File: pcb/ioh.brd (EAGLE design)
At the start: 100 x 80 mm, 11 parts, among them Q1 MOSFET-NCHANNEL2N7000

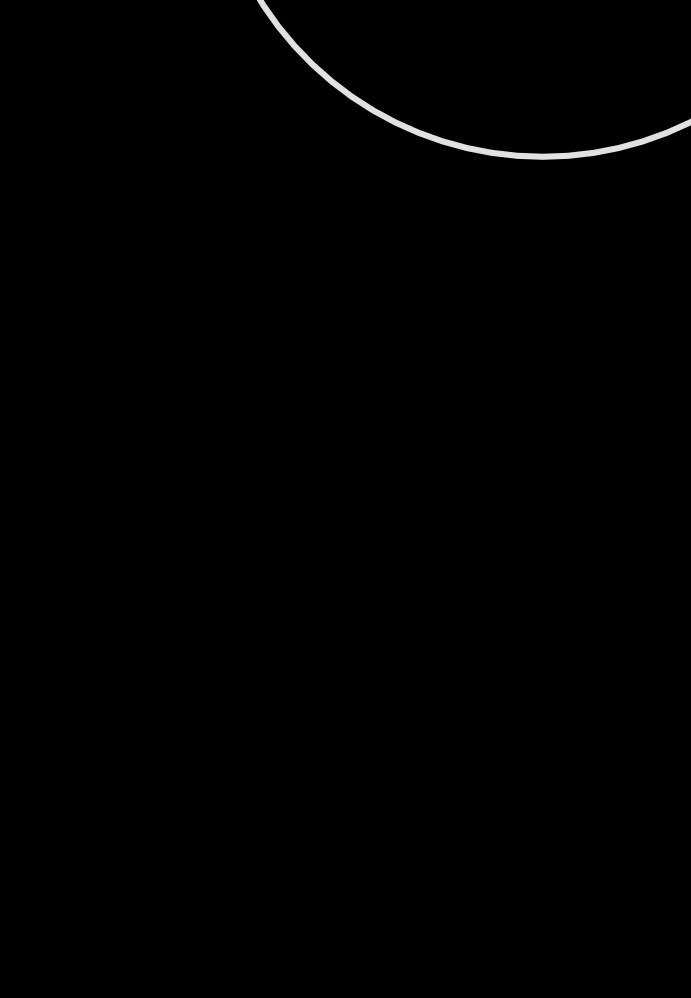
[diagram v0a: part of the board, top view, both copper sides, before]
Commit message: add front/back tx
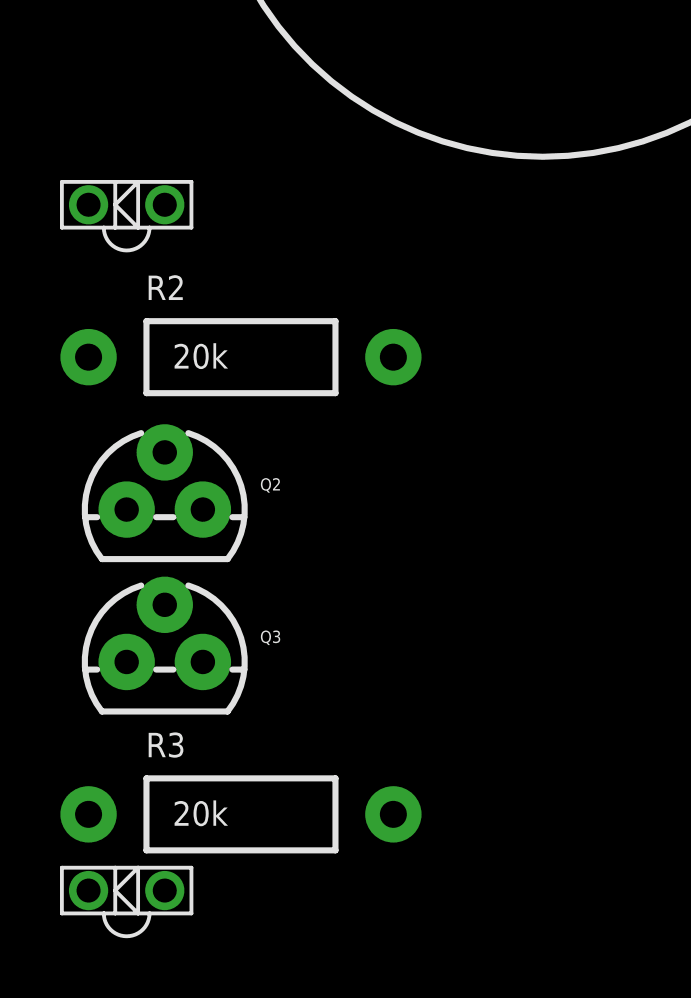
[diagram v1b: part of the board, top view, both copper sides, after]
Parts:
- added D1, D2: (no value), SparkFun-LED:LTE-302
- added Q2, Q3: MOSFET-NCHANNEL2N7000, SparkFun-DiscreteSemi:TO-92
- added R2, R3: 20k, SparkFun-Resistors:AXIAL-0.4
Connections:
- new net N$11: D1.C, Q2.3
- new net N$24: D2.A, R3.P$1
- new net N$25: D2.C, Q3.3
- new net N$4: D1.A, R2.P$1
- new net TXBACK: Q3.2
- new net TXFRONT: Q2.2
- net GND: now also Q2.1, Q3.1
- net VCC: now also R2.P$2, R3.P$2
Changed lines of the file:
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@@
 <element name="Q1" library="SparkFun-DiscreteSemi" package="TO-92" value="MOSFET-NCHANNEL2N7000" x="-52.07" y="71.12"/>
 <element name="R1" library="SparkFun-Resistors" package="AXIAL-0.4" value="20k" x="-62.23" y="69.85"/>
+<element name="D1" library="SparkFun-LED" package="LTE-302" value="" x="-66.04" y="-1.27"/>
+<element name="R2" library="SparkFun-Resistors" package="AXIAL-0.4" value="20k" x="-62.23" y="-6.35"/>
+<element name="Q2" library="SparkFun-DiscreteSemi" package="TO-92" value="MOSFET-NCHANNEL2N7000" x="-64.77" y="-11.43"/>
+<element name="D2" library="SparkFun-LED" package="LTE-302" value="" x="-66.04" y="-24.13"/>
+<element name="R3" library="SparkFun-Resistors" package="AXIAL-0.4" value="20k" x="-62.23" y="-21.59"/>
+<element name="Q3" library="SparkFun-DiscreteSemi" package="TO-92" value="MOSFET-NCHANNEL2N7000" x="-64.77" y="-16.51"/>
 </elements>
 <signals>
@@
 <contactref element="LED3" pad="VSS"/>
 <contactref element="Q1" pad="1"/>
+<contactref element="Q2" pad="1"/>
+<contactref element="Q3" pad="1"/>
+<wire x1="-66.04" y1="-11.43" x2="-66.04" y2="-16.51" width="0" layer="19" extent="1-1"/>
+<wire x1="-60.22" y1="11.43" x2="-66.04" y2="-11.43" width="0" layer="19" extent="1-1"/>
 <wire x1="-36.4" y1="9.62" x2="-60.22" y2="11.43" width="0" layer="19" extent="1-1"/>
 <wire x1="-60.42" y1="38.94" x2="-60.22" y2="11.43" width="0" layer="19" extent="1-1"/>
@@
 <contactref element="LED2" pad="VDD"/>
 <contactref element="R1" pad="P$2"/>
-<wire x1="-21.05" y1="63.5" x2="-17.05" y2="65.2" width="0" layer="19" extent="1-1"/>
-<wire x1="-25.94" y1="65.2" x2="-21.05" y2="63.5" width="0" layer="19" extent="1-1"/>
-<wire x1="-29.94" y1="63.5" x2="-25.94" y2="65.2" width="0" layer="19" extent="1-1"/>
+<contactref element="R2" pad="P$2"/>
+<contactref element="R3" pad="P$2"/>
+<wire x1="-57.15" y1="-6.35" x2="-57.15" y2="-21.59" width="0" layer="19" extent="1-1"/>
+<wire x1="-60.42" y1="40.64" x2="-57.15" y2="-6.35" width="0" layer="19" extent="1-1"/>
+<wire x1="-56.42" y1="42.34" x2="-60.42" y2="40.64" width="0" layer="19" extent="1-1"/>
+<wire x1="-51.53" y1="40.64" x2="-56.42" y2="42.34" width="0" layer="19" extent="1-1"/>
+<wire x1="-47.53" y1="42.34" x2="-51.53" y2="40.64" width="0" layer="19" extent="1-1"/>
+<wire x1="-29.94" y1="63.5" x2="-47.53" y2="42.34" width="0" layer="19" extent="1-1"/>
+<wire x1="-25.94" y1="65.2" x2="-29.94" y2="63.5" width="0" layer="19" extent="1-1"/>
+<wire x1="-21.05" y1="63.5" x2="-25.94" y2="65.2" width="0" layer="19" extent="1-1"/>
+<wire x1="-17.05" y1="65.2" x2="-21.05" y2="63.5" width="0" layer="19" extent="1-1"/>
 <wire x1="-14.82" y1="46.99" x2="-21.05" y2="63.5" width="0" layer="19" extent="1-1"/>
-<wire x1="-47.53" y1="42.34" x2="-29.94" y2="63.5" width="0" layer="19" extent="1-1"/>
-<wire x1="-51.53" y1="40.64" x2="-47.53" y2="42.34" width="0" layer="19" extent="1-1"/>
-<wire x1="-56.42" y1="42.34" x2="-51.53" y2="40.64" width="0" layer="19" extent="1-1"/>
-<wire x1="-60.42" y1="40.64" x2="-56.42" y2="42.34" width="0" layer="19" extent="1-1"/>
 <wire x1="-57.15" y1="69.85" x2="-56.42" y2="42.34" width="0" layer="19" extent="1-1"/>
 </signal>
@@
 <wire x1="-47.53" y1="40.64" x2="-50.8" y2="71.12" width="0" layer="19" extent="1-1"/>
 </signal>
+<signal name="N$4">
+<contactref element="R2" pad="P$1"/>
+<contactref element="D1" pad="A"/>
+<wire x1="-64.77" y1="-1.27" x2="-67.31" y2="-6.35" width="0" layer="19" extent="1-1"/>
+</signal>
+<signal name="N$11">
+<contactref element="D1" pad="C"/>
+<contactref element="Q2" pad="3"/>
+<wire x1="-67.31" y1="-1.27" x2="-63.5" y2="-11.43" width="0" layer="19" extent="1-1"/>
+</signal>
+<signal name="TXBACK">
+<contactref element="Q3" pad="2"/>
+</signal>
+<signal name="N$24">
+<contactref element="R3" pad="P$1"/>
+<contactref element="D2" pad="A"/>
+<wire x1="-64.77" y1="-24.13" x2="-67.31" y2="-21.59" width="0" layer="19" extent="1-1"/>
+</signal>
+<signal name="N$25">
+<contactref element="D2" pad="C"/>
+<contactref element="Q3" pad="3"/>
+<wire x1="-63.5" y1="-16.51" x2="-67.31" y2="-24.13" width="0" layer="19" extent="1-1"/>
+</signal>
+<signal name="TXFRONT">
+<contactref element="Q2" pad="2"/>
+</signal>
 </signals>

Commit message: tsop library addition; placement
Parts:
- added RXBACK, RXFRONT: TSOP2438, ioh-1:TSOP2438
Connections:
- new net RXBACK: RXBACK.OUT
- new net RXFRONT: RXFRONT.OUT
- net GND: now also RXBACK.GND, RXFRONT.GND
- net VCCIO: now also RXBACK.VS, RXFRONT.VS
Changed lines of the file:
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@@
 <element name="R3" library="SparkFun-Resistors" package="AXIAL-0.4" value="20k" x="-62.23" y="-21.59"/>
 <element name="Q3" library="SparkFun-DiscreteSemi" package="TO-92" value="MOSFET-NCHANNEL2N7000" x="-64.77" y="-16.51"/>
+<element name="RXFRONT" library="ioh-1" package="TSOP2438" value="TSOP2438" x="-63.5" y="-27.94"/>
+<element name="RXBACK" library="ioh-1" package="TSOP2438" value="TSOP2438" x="-63.5" y="-33.02"/>
 </elements>
 <signals>
@@
 <contactref element="Q2" pad="1"/>
 <contactref element="Q3" pad="1"/>
+<contactref element="RXFRONT" pad="GND"/>
+<contactref element="RXFRONT" pad="GND"/>
+<contactref element="RXBACK" pad="GND"/>
+<contactref element="RXBACK" pad="GND"/>
+<wire x1="-63.5" y1="-27.94" x2="-63.5" y2="-33.02" width="0" layer="19" extent="1-1"/>
+<wire x1="-66.04" y1="-16.51" x2="-63.5" y2="-27.94" width="0" layer="19" extent="1-1"/>
 <wire x1="-66.04" y1="-11.43" x2="-66.04" y2="-16.51" width="0" layer="19" extent="1-1"/>
 <wire x1="-60.22" y1="11.43" x2="-66.04" y2="-11.43" width="0" layer="19" extent="1-1"/>
@@
 <contactref element="JP1" pad="1"/>
 <contactref element="U$1" pad="1"/>
+<contactref element="RXFRONT" pad="VS"/>
+<contactref element="RXBACK" pad="VS"/>
+<wire x1="-60.96" y1="-27.94" x2="-60.96" y2="-33.02" width="0" layer="19" extent="1-1"/>
+<wire x1="-40.22" y1="11.43" x2="-60.96" y2="-27.94" width="0" layer="19" extent="1-1"/>
 <wire x1="-36.4" y1="27.62" x2="-40.22" y2="11.43" width="0" layer="19" extent="1-1"/>
 <wire x1="-34.82" y1="46.99" x2="-36.4" y2="27.62" width="0" layer="19" extent="1-1"/>
@@
 <contactref element="Q2" pad="2"/>
 </signal>
+<signal name="RXFRONT">
+<contactref element="RXFRONT" pad="OUT"/>
+</signal>
+<signal name="RXBACK">
+<contactref element="RXBACK" pad="OUT"/>
+</signal>
 </signals>

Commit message: vibe placement; update todo; caps
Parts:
- added C1: 10uF, SparkFun-Capacitors:CPOL-RADIAL-10UF-25V-KIT
- added JP3: M02PTH, SparkFun-Connectors:1X02
- added Q4: MOSFET-NCHANNEL2N7000, SparkFun-DiscreteSemi:TO-92
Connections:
- new net N$13: JP3.2, Q4.3
- new net VIBE: Q4.2
- net GND: now also C1.2, Q4.1
- net VCC: now also JP3.1
- net VCCIO: now also C1.1
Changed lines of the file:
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@@
 <element name="RXFRONT" library="ioh-1" package="TSOP2438" value="TSOP2438" x="-63.5" y="-27.94"/>
 <element name="RXBACK" library="ioh-1" package="TSOP2438" value="TSOP2438" x="-63.5" y="-33.02"/>
+<element name="C1" library="SparkFun-Capacitors" package="CPOL-RADIAL-10UF-25V-KIT" value="10uF" x="-72.39" y="-30.48">
+<attribute name="PROD_ID" value="CAP-08440" x="-72.39" y="-30.48" size="1.778" layer="27" display="off"/>
+</element>
+<element name="JP3" library="SparkFun-Connectors" package="1X02" value="M02PTH" x="-72.39" y="-39.37"/>
+<element name="Q4" library="SparkFun-DiscreteSemi" package="TO-92" value="MOSFET-NCHANNEL2N7000" x="-71.12" y="-46.99"/>
 </elements>
 <signals>
@@
 <contactref element="RXBACK" pad="GND"/>
 <contactref element="RXBACK" pad="GND"/>
+<contactref element="C1" pad="2"/>
+<contactref element="Q4" pad="1"/>
+<wire x1="-73.66" y1="-30.48" x2="-72.39" y2="-46.99" width="0" layer="19" extent="1-1"/>
+<wire x1="-63.5" y1="-33.02" x2="-73.66" y2="-30.48" width="0" layer="19" extent="1-1"/>
 <wire x1="-63.5" y1="-27.94" x2="-63.5" y2="-33.02" width="0" layer="19" extent="1-1"/>
 <wire x1="-66.04" y1="-16.51" x2="-63.5" y2="-27.94" width="0" layer="19" extent="1-1"/>
@@
 <contactref element="RXFRONT" pad="VS"/>
 <contactref element="RXBACK" pad="VS"/>
+<contactref element="C1" pad="1"/>
+<wire x1="-60.96" y1="-33.02" x2="-71.12" y2="-30.48" width="0" layer="19" extent="1-1"/>
 <wire x1="-60.96" y1="-27.94" x2="-60.96" y2="-33.02" width="0" layer="19" extent="1-1"/>
 <wire x1="-40.22" y1="11.43" x2="-60.96" y2="-27.94" width="0" layer="19" extent="1-1"/>
@@
 <contactref element="R2" pad="P$2"/>
 <contactref element="R3" pad="P$2"/>
+<contactref element="JP3" pad="1"/>
+<wire x1="-57.15" y1="-21.59" x2="-72.39" y2="-39.37" width="0" layer="19" extent="1-1"/>
 <wire x1="-57.15" y1="-6.35" x2="-57.15" y2="-21.59" width="0" layer="19" extent="1-1"/>
 <wire x1="-60.42" y1="40.64" x2="-57.15" y2="-6.35" width="0" layer="19" extent="1-1"/>
@@
 <contactref element="RXBACK" pad="OUT"/>
 </signal>
+<signal name="N$13">
+<contactref element="Q4" pad="3"/>
+<contactref element="JP3" pad="2"/>
+<wire x1="-69.85" y1="-39.37" x2="-69.85" y2="-46.99" width="0" layer="19" extent="1-1"/>
+</signal>
+<signal name="VIBE">
+<contactref element="Q4" pad="2"/>
+</signal>
 </signals>

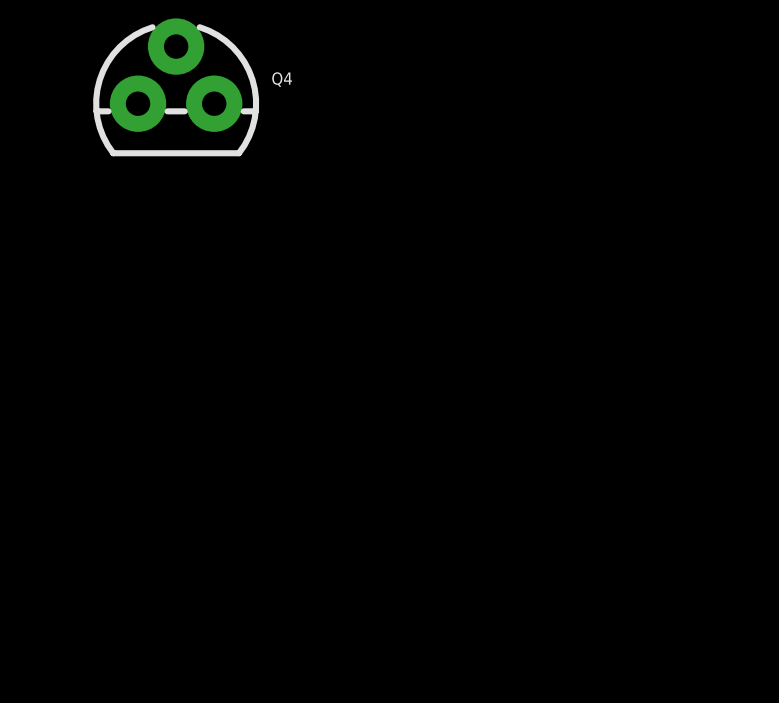
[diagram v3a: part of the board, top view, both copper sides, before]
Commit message: add switch
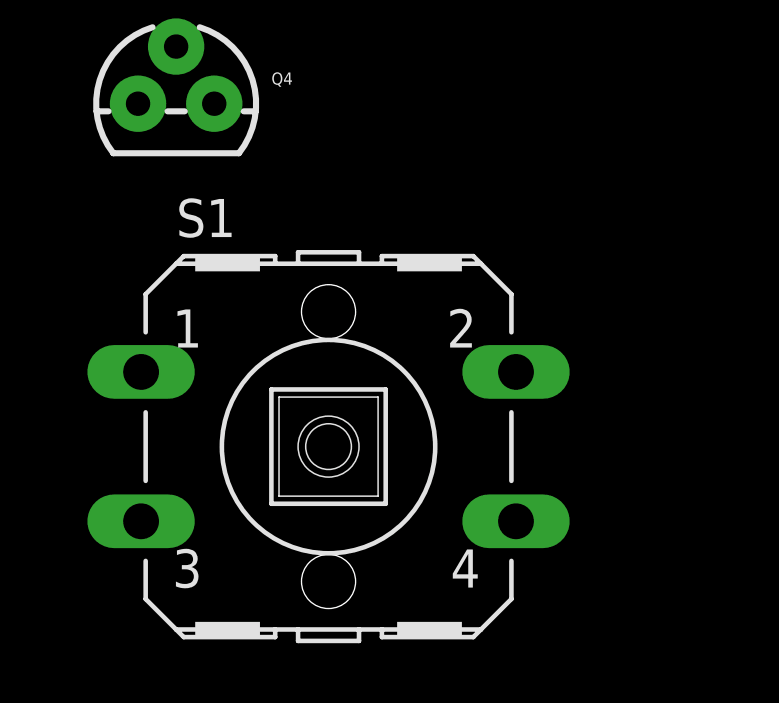
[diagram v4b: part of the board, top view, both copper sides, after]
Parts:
- added S1: (no value), adafruit:B3F-40XX
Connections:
- new net BOOP: S1.1, S1.2
- net GND: now also S1.3, S1.4
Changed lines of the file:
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@@
 <element name="JP3" library="SparkFun-Connectors" package="1X02" value="M02PTH" x="-72.39" y="-39.37"/>
 <element name="Q4" library="SparkFun-DiscreteSemi" package="TO-92" value="MOSFET-NCHANNEL2N7000" x="-71.12" y="-46.99"/>
+<element name="S1" library="adafruit" package="B3F-40XX" value="" x="-66.04" y="-58.42">
+<attribute name="OC_NEWARK" value="36K3105" x="-66.04" y="-58.42" size="1.778" layer="27" display="off"/>
+<attribute name="MPN" value="B3F-4000" x="-66.04" y="-58.42" size="1.778" layer="27" display="off"/>
+<attribute name="MF" value="OMRON COMPONENTS USA" x="-66.04" y="-58.42" size="1.778" layer="27" display="off"/>
+<attribute name="OC_FARNELL" value="176434" x="-66.04" y="-58.42" size="1.778" layer="27" display="off"/>
+</element>
 </elements>
 <signals>
@@
 <contactref element="C1" pad="2"/>
 <contactref element="Q4" pad="1"/>
+<contactref element="S1" pad="3"/>
+<contactref element="S1" pad="4"/>
+<wire x1="-59.7916" y1="-60.9092" x2="-72.2884" y2="-60.9092" width="0" layer="19" extent="1-1"/>
+<wire x1="-72.39" y1="-46.99" x2="-72.2884" y2="-60.9092" width="0" layer="19" extent="1-1"/>
 <wire x1="-73.66" y1="-30.48" x2="-72.39" y2="-46.99" width="0" layer="19" extent="1-1"/>
 <wire x1="-63.5" y1="-33.02" x2="-73.66" y2="-30.48" width="0" layer="19" extent="1-1"/>
@@
 <contactref element="Q4" pad="2"/>
 </signal>
+<signal name="BOOP">
+<contactref element="S1" pad="1"/>
+<contactref element="S1" pad="2"/>
+<wire x1="-59.7916" y1="-55.9308" x2="-72.2884" y2="-55.9308" width="0" layer="19" extent="1-1"/>
+</signal>
 </signals>

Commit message: actually connect things
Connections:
- removed net N$15: JP2.2, U$1.12
- removed net N$17: JP2.4, U$1.14
- removed net N$20: JP2.7, U$1.17
- removed net N$21: JP2.8, U$1.18
- removed net N$6: JP1.3, U$1.3
- net RXBACK: now also JP2.4, U$1.14
- net RXFRONT: now also JP1.3, U$1.3
- net TXBACK: now also JP2.7, U$1.17
- net TXFRONT: now also JP2.8, U$1.18
- net VIBE: now also JP2.2, U$1.12
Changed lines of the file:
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@@
 <wire x1="-53.34" y1="62.23" x2="-36.4" y2="25.62" width="0" layer="19" extent="1-1"/>
-</signal>
-<signal name="N$6">
-<contactref element="JP1" pad="3"/>
-<contactref element="U$1" pad="3"/>
-<wire x1="-50.8" y1="62.23" x2="-36.4" y2="23.62" width="0" layer="19" extent="1-1"/>
 </signal>
 <signal name="N$7">
@@
 <wire x1="-14.4" y1="9.62" x2="-38.1" y2="72.39" width="0" layer="19" extent="1-1"/>
 </signal>
-<signal name="N$15">
-<contactref element="U$1" pad="12"/>
-<contactref element="JP2" pad="2"/>
-<wire x1="-14.4" y1="11.62" x2="-35.56" y2="72.39" width="0" layer="19" extent="1-1"/>
-</signal>
 <signal name="N$16">
 <contactref element="U$1" pad="13"/>
@@
 <wire x1="-14.4" y1="13.62" x2="-33.02" y2="72.39" width="0" layer="19" extent="1-1"/>
 </signal>
-<signal name="N$17">
-<contactref element="U$1" pad="14"/>
-<contactref element="JP2" pad="4"/>
-<wire x1="-14.4" y1="15.62" x2="-30.48" y2="72.39" width="0" layer="19" extent="1-1"/>
-</signal>
 <signal name="N$18">
 <contactref element="U$1" pad="15"/>
@@
 <contactref element="JP2" pad="6"/>
 <wire x1="-14.4" y1="19.62" x2="-25.4" y2="72.39" width="0" layer="19" extent="1-1"/>
-</signal>
-<signal name="N$20">
-<contactref element="U$1" pad="17"/>
-<contactref element="JP2" pad="7"/>
-<wire x1="-14.4" y1="21.62" x2="-22.86" y2="72.39" width="0" layer="19" extent="1-1"/>
-</signal>
-<signal name="N$21">
-<contactref element="U$1" pad="18"/>
-<contactref element="JP2" pad="8"/>
-<wire x1="-14.4" y1="23.62" x2="-20.32" y2="72.39" width="0" layer="19" extent="1-1"/>
 </signal>
 <signal name="N$22">
@@
 <signal name="TXBACK">
 <contactref element="Q3" pad="2"/>
+<contactref element="U$1" pad="17"/>
+<contactref element="JP2" pad="7"/>
+<wire x1="-14.4" y1="21.62" x2="-64.77" y2="-14.605" width="0" layer="19" extent="1-1"/>
+<wire x1="-22.86" y1="72.39" x2="-14.4" y2="21.62" width="0" layer="19" extent="1-1"/>
 </signal>
 <signal name="N$24">
@@
 <signal name="TXFRONT">
 <contactref element="Q2" pad="2"/>
+<contactref element="U$1" pad="18"/>
+<contactref element="JP2" pad="8"/>
+<wire x1="-14.4" y1="23.62" x2="-64.77" y2="-9.525" width="0" layer="19" extent="1-1"/>
+<wire x1="-20.32" y1="72.39" x2="-14.4" y2="23.62" width="0" layer="19" extent="1-1"/>
 </signal>
 <signal name="RXFRONT">
 <contactref element="RXFRONT" pad="OUT"/>
+<contactref element="JP1" pad="3"/>
+<contactref element="U$1" pad="3"/>
+<wire x1="-36.4" y1="23.62" x2="-66.04" y2="-27.94" width="0" layer="19" extent="1-1"/>
+<wire x1="-50.8" y1="62.23" x2="-36.4" y2="23.62" width="0" layer="19" extent="1-1"/>
 </signal>
 <signal name="RXBACK">
 <contactref element="RXBACK" pad="OUT"/>
+<contactref element="U$1" pad="14"/>
+<contactref element="JP2" pad="4"/>
+<wire x1="-14.4" y1="15.62" x2="-66.04" y2="-33.02" width="0" layer="19" extent="1-1"/>
+<wire x1="-30.48" y1="72.39" x2="-14.4" y2="15.62" width="0" layer="19" extent="1-1"/>
 </signal>
 <signal name="N$13">
@@
 <signal name="VIBE">
 <contactref element="Q4" pad="2"/>
+<contactref element="U$1" pad="12"/>
+<contactref element="JP2" pad="2"/>
+<wire x1="-14.4" y1="11.62" x2="-71.12" y2="-45.085" width="0" layer="19" extent="1-1"/>
+<wire x1="-35.56" y1="72.39" x2="-14.4" y2="11.62" width="0" layer="19" extent="1-1"/>
 </signal>
 <signal name="BOOP">
